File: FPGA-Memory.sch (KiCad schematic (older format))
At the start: 6 parts, among them U31 MX25R8035FM1IH1, U32 APS6404L-SQN-SN, U33 APS6404L-SQN-SN

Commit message: PVT
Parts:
- U29: renamed from U31; value MX25R8035FM1IH1 -> GD25LQ16CTIGR; PartName MX25R8035FM1IH1 -> GD25LQ16CTIGR
- renumbered C128 to C123, C129 to C124, C130 to C125, U32 to U30, U33 to U31
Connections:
- net ~FLASH_CSO renamed ~FLASH_CS
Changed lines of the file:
@@
 encoding utf-8
 Sheet 14 24
-Title "Phoenix DVT"
-Date "2020-05-18"
+Title "Phoenix PVT"
+Date "2020-07-19"
 Rev "1"
 Comp ""
@@
 $EndDescr
 Text HLabel 3300 3500 2    50   Input ~ 0
-~FLASH_CSO
+~FLASH_CS
 Text HLabel 3300 3700 2    50   Input ~ 0
 FLASH_DCLK
@@
 P 1600 4000
 AR Path="/5E4B5786/5ED218FC" Ref="C?"  Part="1"
-AR Path="/5E4B5786/5ECCB01D/5ED218FC" Ref="C128"  Part="1"
-F 0 "C128" H 1700 4050 50  0000 L CNN
+AR Path="/5E4B5786/5ECCB01D/5ED218FC" Ref="C123"  Part="1"
+F 0 "C123" H 1700 4050 50  0000 L CNN
 F 1 "100n" H 1700 3950 50  0000 L CNN
 F 2 "Capacitor-Chip:C_CHIP_1005_Hand_NoSilk" H 1700 3900 50  0001 C CNN
@@
 P 1600 4500
 AR Path="/5E4B5786/5ED21903" Ref="#PWR?"  Part="1"
-AR Path="/5E4B5786/5ECCB01D/5ED21903" Ref="#PWR0283"  Part="1"
-F 0 "#PWR0283" H 1600 4250 50  0001 C CNN
+AR Path="/5E4B5786/5ECCB01D/5ED21903" Ref="#PWR0271"  Part="1"
+F 0 "#PWR0271" H 1600 4250 50  0001 C CNN
 F 1 "GND" H 1600 4350 50  0000 C CNN
 F 2 "" H 1600 4500 50  0001 C CNN
@@
 P 2500 4000
 AR Path="/5E4B5786/5ED2190A" Ref="U?"  Part="1"
-AR Path="/5E4B5786/5ECCB01D/5ED2190A" Ref="U31"  Part="1"
-F 0 "U31" H 2500 4650 50  0000 C CNN
-F 1 "MX25R8035FM1IH1" H 2500 3350 50  0000 C CNN
+AR Path="/5E4B5786/5ECCB01D/5ED2190A" Ref="U29"  Part="1"
+F 0 "U29" H 2500 4650 50  0000 C CNN
+F 1 "GD25LQ16CTIGR" H 2500 3350 50  0000 C CNN
 F 2 "IC-SOP:SOP8-W3.9" H 2500 4000 50  0001 C CNN
 F 3 "" H 2500 4000 50  0001 C CNN
-F 4 "MX25R8035FM1IH1" H 2500 4000 50  0001 C CNN "PartName"
+F 4 "GD25LQ16CTIGR" H 2500 4000 50  0001 C CNN "PartName"
 	1    2500 4000
 	1    0    0    -1
@@
 P 1600 3500
 AR Path="/5E4B5786/5ED21915" Ref="#PWR?"  Part="1"
-AR Path="/5E4B5786/5ECCB01D/5ED21915" Ref="#PWR0282"  Part="1"
-F 0 "#PWR0282" H 1600 3350 50  0001 C CNN
+AR Path="/5E4B5786/5ECCB01D/5ED21915" Ref="#PWR0270"  Part="1"
+F 0 "#PWR0270" H 1600 3350 50  0001 C CNN
 F 1 "+1V8" H 1600 3640 50  0000 C CNN
 F 2 "" H 1600 3500 50  0001 C CNN
@@
 P 6000 4000
 AR Path="/5E4B5786/5EFD51B9" Ref="U?"  Part="1"
-AR Path="/5E4B5786/5ECCB01D/5EFD51B9" Ref="U32"  Part="1"
-F 0 "U32" H 6000 4650 50  0000 C CNN
+AR Path="/5E4B5786/5ECCB01D/5EFD51B9" Ref="U30"  Part="1"
+F 0 "U30" H 6000 4650 50  0000 C CNN
 F 1 "APS6404L-SQN-SN" H 6000 3350 50  0000 C CNN
 F 2 "IC-SOP:SOP8-W3.9" H 6000 4000 50  0001 C CNN
@@
 P 5100 4000
 AR Path="/5E4B5786/5EFD51C2" Ref="C?"  Part="1"
-AR Path="/5E4B5786/5ECCB01D/5EFD51C2" Ref="C129"  Part="1"
-F 0 "C129" H 5200 4050 50  0000 L CNN
+AR Path="/5E4B5786/5ECCB01D/5EFD51C2" Ref="C124"  Part="1"
+F 0 "C124" H 5200 4050 50  0000 L CNN
 F 1 "100n" H 5200 3950 50  0000 L CNN
 F 2 "Capacitor-Chip:C_CHIP_1005_Hand_NoSilk" H 5200 3900 50  0001 C CNN
@@
 P 5100 4500
 AR Path="/5E4B5786/5EFD51C9" Ref="#PWR?"  Part="1"
-AR Path="/5E4B5786/5ECCB01D/5EFD51C9" Ref="#PWR0284"  Part="1"
-F 0 "#PWR0284" H 5100 4250 50  0001 C CNN
+AR Path="/5E4B5786/5ECCB01D/5EFD51C9" Ref="#PWR0272"  Part="1"
+F 0 "#PWR0272" H 5100 4250 50  0001 C CNN
 F 1 "GND" H 5100 4350 50  0000 C CNN
 F 2 "" H 5100 4500 50  0001 C CNN
@@
 Wire Wire Line
 	6600 4500 6800 4500
+Wire Wire Line
+	8600 3900 8600 3500
+Connection ~ 8600 4500
+Wire Wire Line
+	8600 4100 8600 4500
+$Comp
+L passive:C C?
+U 1 1 5F09B55F
+P 8600 4000
+AR Path="/5E4B5786/5F09B55F" Ref="C?"  Part="1"
+AR Path="/5E4B5786/5ECCB01D/5F09B55F" Ref="C125"  Part="1"
+F 0 "C125" H 8700 4050 50  0000 L CNN
+F 1 "100n" H 8700 3950 50  0000 L CNN
+F 2 "Capacitor-Chip:C_CHIP_1005_Hand_NoSilk" H 8700 3900 50  0001 C CNN
+F 3 "" H 8625 4100 50  0001 C CNN
+F 4 "GRM155R71H104ME14D" H 8600 4000 50  0001 C CNN "PartName"
+	1    8600 4000
+	1    0    0    -1
+$EndComp
+Wire Wire Line
+	8600 4500 8900 4500
+$Comp
+L supply-alias:GND #PWR?
+U 1 1 5F09B566
+P 8600 4500
+AR Path="/5E4B5786/5F09B566" Ref="#PWR?"  Part="1"
+AR Path="/5E4B5786/5ECCB01D/5F09B566" Ref="#PWR0273"  Part="1"
+F 0 "#PWR0273" H 8600 4250 50  0001 C CNN
+F 1 "GND" H 8600 4350 50  0000 C CNN
+F 2 "" H 8600 4500 50  0001 C CNN
+F 3 "" H 8600 4500 50  0001 C CNN
+	1    8600 4500
+	1    0    0    -1
+$EndComp
+Wire Wire Line
+	8600 3500 8900 3500
+Wire Wire Line
+	10100 3500 10300 3500
+Wire Wire Line
+	10100 3700 10300 3700
+Wire Wire Line
+	10100 3900 10300 3900
+Wire Wire Line
+	10100 4100 10300 4100
+Wire Wire Line
+	10100 4300 10300 4300
+Wire Wire Line
+	10100 4500 10300 4500
+Text Notes 5600 4900 0    50   ~ 0
+PSRAMs are reserved for future use.
 $Comp
 L memory:APSxx04x-x-SN U?
@@
 P 9500 4000
 AR Path="/5E4B5786/5F09B556" Ref="U?"  Part="1"
-AR Path="/5E4B5786/5ECCB01D/5F09B556" Ref="U33"  Part="1"
-F 0 "U33" H 9500 4650 50  0000 C CNN
+AR Path="/5E4B5786/5ECCB01D/5F09B556" Ref="U31"  Part="1"
+F 0 "U31" H 9500 4650 50  0000 C CNN
 F 1 "APS6404L-SQN-SN" H 9500 3350 50  0000 C CNN
 F 2 "IC-SOP:SOP8-W3.9" H 9500 4000 50  0001 C CNN
@@
 	1    0    0    -1
 $EndComp
-Wire Wire Line
-	8600 3900 8600 3500
-Connection ~ 8600 4500
-Wire Wire Line
-	8600 4100 8600 4500
-$Comp
-L passive:C C?
-U 1 1 5F09B55F
-P 8600 4000
-AR Path="/5E4B5786/5F09B55F" Ref="C?"  Part="1"
-AR Path="/5E4B5786/5ECCB01D/5F09B55F" Ref="C130"  Part="1"
-F 0 "C130" H 8700 4050 50  0000 L CNN
-F 1 "100n" H 8700 3950 50  0000 L CNN
-F 2 "Capacitor-Chip:C_CHIP_1005_Hand_NoSilk" H 8700 3900 50  0001 C CNN
-F 3 "" H 8625 4100 50  0001 C CNN
-F 4 "GRM155R71H104ME14D" H 8600 4000 50  0001 C CNN "PartName"
-	1    8600 4000
-	1    0    0    -1
-$EndComp
-Wire Wire Line
-	8600 4500 8900 4500
-$Comp
-L supply-alias:GND #PWR?
-U 1 1 5F09B566
-P 8600 4500
-AR Path="/5E4B5786/5F09B566" Ref="#PWR?"  Part="1"
-AR Path="/5E4B5786/5ECCB01D/5F09B566" Ref="#PWR0285"  Part="1"
-F 0 "#PWR0285" H 8600 4250 50  0001 C CNN
-F 1 "GND" H 8600 4350 50  0000 C CNN
-F 2 "" H 8600 4500 50  0001 C CNN
-F 3 "" H 8600 4500 50  0001 C CNN
-	1    8600 4500
-	1    0    0    -1
-$EndComp
-Wire Wire Line
-	8600 3500 8900 3500
-Wire Wire Line
-	10100 3500 10300 3500
-Wire Wire Line
-	10100 3700 10300 3700
-Wire Wire Line
-	10100 3900 10300 3900
-Wire Wire Line
-	10100 4100 10300 4100
-Wire Wire Line
-	10100 4300 10300 4300
-Wire Wire Line
-	10100 4500 10300 4500
+Connection ~ 8600 3500
+Wire Wire Line
+	8600 3000 8600 3500
+Wire Wire Line
+	5100 3000 8600 3000
+Connection ~ 5100 3500
+Wire Wire Line
+	5100 3500 5100 3000
+Connection ~ 5100 3000
+Wire Wire Line
+	4900 3000 5100 3000
 Text HLabel 4900 3000 0    50   Input ~ 0
 VCCIO
-Wire Wire Line
-	4900 3000 5100 3000
-Connection ~ 5100 3500
-Wire Wire Line
-	5100 3500 5100 3000
-Wire Wire Line
-	5100 3000 8600 3000
-Wire Wire Line
-	8600 3000 8600 3500
-Connection ~ 8600 3500
-Connection ~ 5100 3000
-Text Notes 5600 4900 0    50   ~ 0
-PSRAMs are reserved for future use.
 $EndSCHEMATC

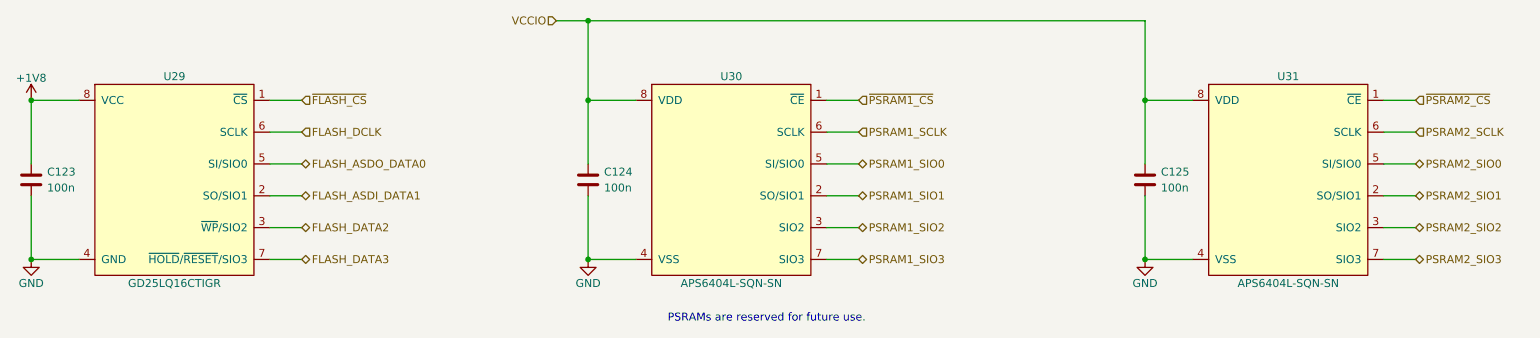
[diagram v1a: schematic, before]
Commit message: SBUにTVSダイオードを追加
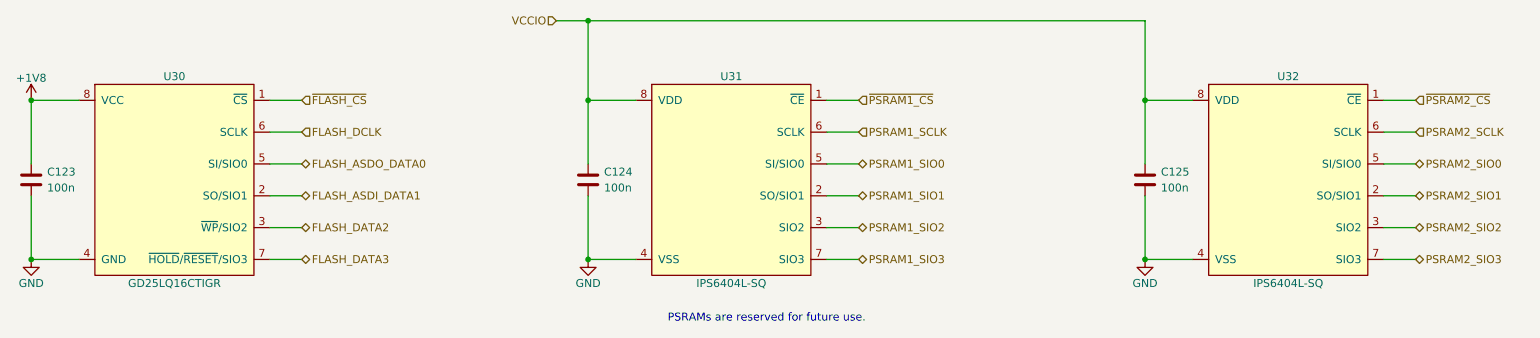
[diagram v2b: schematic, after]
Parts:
- U31: renamed from U30; value APS6404L-SQN-SN -> IPS6404L-SQ; PartName APS6404L-SQN-SN -> IPS6404L-SQ
- U32: renamed from U31; value APS6404L-SQN-SN -> IPS6404L-SQ; PartName APS6404L-SQN-SN -> IPS6404L-SQ
- renumbered U29 to U30
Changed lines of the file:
@@
 P 2500 4000
 AR Path="/5E4B5786/5ED2190A" Ref="U?"  Part="1"
-AR Path="/5E4B5786/5ECCB01D/5ED2190A" Ref="U29"  Part="1"
-F 0 "U29" H 2500 4650 50  0000 C CNN
+AR Path="/5E4B5786/5ECCB01D/5ED2190A" Ref="U30"  Part="1"
+F 0 "U30" H 2500 4650 50  0000 C CNN
 F 1 "GD25LQ16CTIGR" H 2500 3350 50  0000 C CNN
 F 2 "IC-SOP:SOP8-W3.9" H 2500 4000 50  0001 C CNN
@@
 P 6000 4000
 AR Path="/5E4B5786/5EFD51B9" Ref="U?"  Part="1"
-AR Path="/5E4B5786/5ECCB01D/5EFD51B9" Ref="U30"  Part="1"
-F 0 "U30" H 6000 4650 50  0000 C CNN
-F 1 "APS6404L-SQN-SN" H 6000 3350 50  0000 C CNN
+AR Path="/5E4B5786/5ECCB01D/5EFD51B9" Ref="U31"  Part="1"
+F 0 "U31" H 6000 4650 50  0000 C CNN
+F 1 "IPS6404L-SQ" H 6000 3350 50  0000 C CNN
 F 2 "IC-SOP:SOP8-W3.9" H 6000 4000 50  0001 C CNN
 F 3 "" H 6000 4000 50  0001 C CNN
 F 4 "None" H 6000 4000 50  0001 C CNN "Supplier"
-F 5 "APS6404L-SQN-SN" H 6000 4000 50  0001 C CNN "PartName"
+F 5 "IPS6404L-SQ" H 6000 4000 50  0001 C CNN "PartName"
 	1    6000 4000
 	1    0    0    -1
@@
 P 9500 4000
 AR Path="/5E4B5786/5F09B556" Ref="U?"  Part="1"
-AR Path="/5E4B5786/5ECCB01D/5F09B556" Ref="U31"  Part="1"
-F 0 "U31" H 9500 4650 50  0000 C CNN
-F 1 "APS6404L-SQN-SN" H 9500 3350 50  0000 C CNN
+AR Path="/5E4B5786/5ECCB01D/5F09B556" Ref="U32"  Part="1"
+F 0 "U32" H 9500 4650 50  0000 C CNN
+F 1 "IPS6404L-SQ" H 9500 3350 50  0000 C CNN
 F 2 "IC-SOP:SOP8-W3.9" H 9500 4000 50  0001 C CNN
 F 3 "" H 9500 4000 50  0001 C CNN
 F 4 "None" H 9500 4000 50  0001 C CNN "Supplier"
-F 5 "APS6404L-SQN-SN" H 9500 4000 50  0001 C CNN "PartName"
+F 5 "IPS6404L-SQ" H 9500 4000 50  0001 C CNN "PartName"
 	1    9500 4000
 	1    0    0    -1

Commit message: FPGA_INTをFPGA_MODEに変更
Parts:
- U30: symbol memory:MX25R8035F -> memory:MX25Rxx35F
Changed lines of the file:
@@
 	1600 3500 1900 3500
 $Comp
-L memory:MX25R8035F U?
+L memory:MX25Rxx35F U?
 U 1 1 5ED2190A
 P 2500 4000
